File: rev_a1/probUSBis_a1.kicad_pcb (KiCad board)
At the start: 2 copper layers, 44.5 x 22.9 mm, 23 parts, among them CON1 USB-MINI-B, IC1 ATTINY85-P, P1 USB_A_MALE, P2 CONN_8, P3 CONN_4, U1 LM78L05ACZ

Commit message: moving usb around, fiddling with the pcb
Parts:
- JP1: moved to B.Cu
- moved P1 6.34 mm to (109.8, 100.5)
- moved CON1 4.06 mm to (109.2, 108.0)
- moved JP2 1.79 mm to (128.5, 93.0)
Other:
- board text added: "3.6V"
- board text added: "5V"
- board text added: "P1_LED"
- board text added: "VIN"
- board text added: "Voltage Select ->"
- board text added: "user LED jumper"
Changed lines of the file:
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@@
   (general
     (links 52)
-    (no_connects 52)
-    (area 93.996934 90.096623 152.40127 115.23345)
+    (no_connects 51)
+    (area 95.266934 89.249956 152.40127 115.26478)
     (thickness 1.6)
-    (drawings 12)
+    (drawings 22)
     (tracks 0)
     (zones 0)
@@
   )
   (module USB_MINI_B (layer F.Cu)
-    (at 110.49 104.14)
+    (at 109.22 108)
     (descr "USB Mini-B 5-pin SMD connector")
     (tags "USB, Mini-B, connector")
@@
   )
   (module PIN_ARRAY_3X1 (layer F.Cu)
-    (at 127 93.98)
+    (at 128.5 93)
     (descr "Connecteur 3 pins")
     (tags "CONN DEV")
@@
   )
   (module USB_A (layer F.Cu)
-    (at 111.2 106.68 180)
+    (at 109.8 100.5 180)
     (fp_text reference P1 (at 7.62 2.54 180) (layer F.SilkS)
       (effects (font (thickness 0.3048)))
@@
     )
   )
-  (module SM0603 (layer F.Cu)
+  (module SM0603 (layer B.Cu)
     (at 137.16 104.14 90)
     (attr smd)
-    (fp_text reference JP1 (at 0 0 90) (layer F.SilkS)
-      (effects (font (size 0.508 0.4572) (thickness 0.1143)))
-    )
-    (fp_text value JUMPER (at 0 0 90) (layer F.SilkS) hide
-      (effects (font (size 0.508 0.4572) (thickness 0.1143)))
-    )
-    (fp_line (start -1.143 -0.635) (end 1.143 -0.635) (layer F.SilkS) (width 0.127))
-    (fp_line (start 1.143 -0.635) (end 1.143 0.635) (layer F.SilkS) (width 0.127))
-    (fp_line (start 1.143 0.635) (end -1.143 0.635) (layer F.SilkS) (width 0.127))
-    (fp_line (start -1.143 0.635) (end -1.143 -0.635) (layer F.SilkS) (width 0.127))
+    (fp_text reference JP1 (at 0 0 90) (layer B.SilkS)
+      (effects (font (size 0.508 0.4572) (thickness 0.1143)) (justify mirror))
+    )
+    (fp_text value JUMPER (at 0 0 90) (layer B.SilkS) hide
+      (effects (font (size 0.508 0.4572) (thickness 0.1143)) (justify mirror))
+    )
+    (fp_line (start -1.143 0.635) (end 1.143 0.635) (layer B.SilkS) (width 0.127))
+    (fp_line (start 1.143 0.635) (end 1.143 -0.635) (layer B.SilkS) (width 0.127))
+    (fp_line (start 1.143 -0.635) (end -1.143 -0.635) (layer B.SilkS) (width 0.127))
+    (fp_line (start -1.143 -0.635) (end -1.143 0.635) (layer B.SilkS) (width 0.127))
     (pad 1 smd rect (at -0.762 0 90) (size 0.635 1.143)
-      (layers F.Cu F.Paste F.Mask)
+      (layers B.Cu B.Paste B.Mask)
       (net 16 N-000007)
     )
     (pad 2 smd rect (at 0.762 0 90) (size 0.635 1.143)
-      (layers F.Cu F.Paste F.Mask)
+      (layers B.Cu B.Paste B.Mask)
       (net 4 N-0000010)
     )
@@
     )
   )
+  (gr_text P1_LED (at 139.5 103) (layer F.SilkS)
+    (effects (font (size 1 1) (thickness 0.25)))
+  )
+  (gr_text "Voltage Select ->" (at 120 92.5) (layer F.SilkS)
+    (effects (font (size 0.6 0.6) (thickness 0.1)))
+  )
+  (gr_text 3.6V (at 131.4 95) (layer F.SilkS)
+    (effects (font (size 0.8 0.8) (thickness 0.1)))
+  )
+  (gr_text VCC (at 128.5 95) (layer F.SilkS)
+    (effects (font (size 0.8 0.8) (thickness 0.1)))
+  )
+  (gr_text 5V (at 126 95) (layer F.SilkS)
+    (effects (font (size 0.8 0.8) (thickness 0.1)))
+  )
+  (gr_text VIN (at 143.5 109.8) (layer F.SilkS)
+    (effects (font (size 0.8 0.8) (thickness 0.1)))
+  )
+  (gr_text GND (at 141 109.8) (layer F.SilkS)
+    (effects (font (size 0.8 0.8) (thickness 0.1)))
+  )
+  (gr_text "user LED \njumper" (at 139.7 104.14 270) (layer B.SilkS)
+    (effects (font (size 0.8 0.8) (thickness 0.1)) (justify mirror))
+  )
+  (gr_text 5V (at 138.5 109.9) (layer F.SilkS)
+    (effects (font (size 0.8 0.8) (thickness 0.1)))
+  )
+  (gr_text 3.6V (at 136 109.8) (layer F.SilkS)
+    (effects (font (size 0.8 0.8) (thickness 0.1)))
+  )
   (gr_text VCC (at 146 111.76 90) (layer F.SilkS)

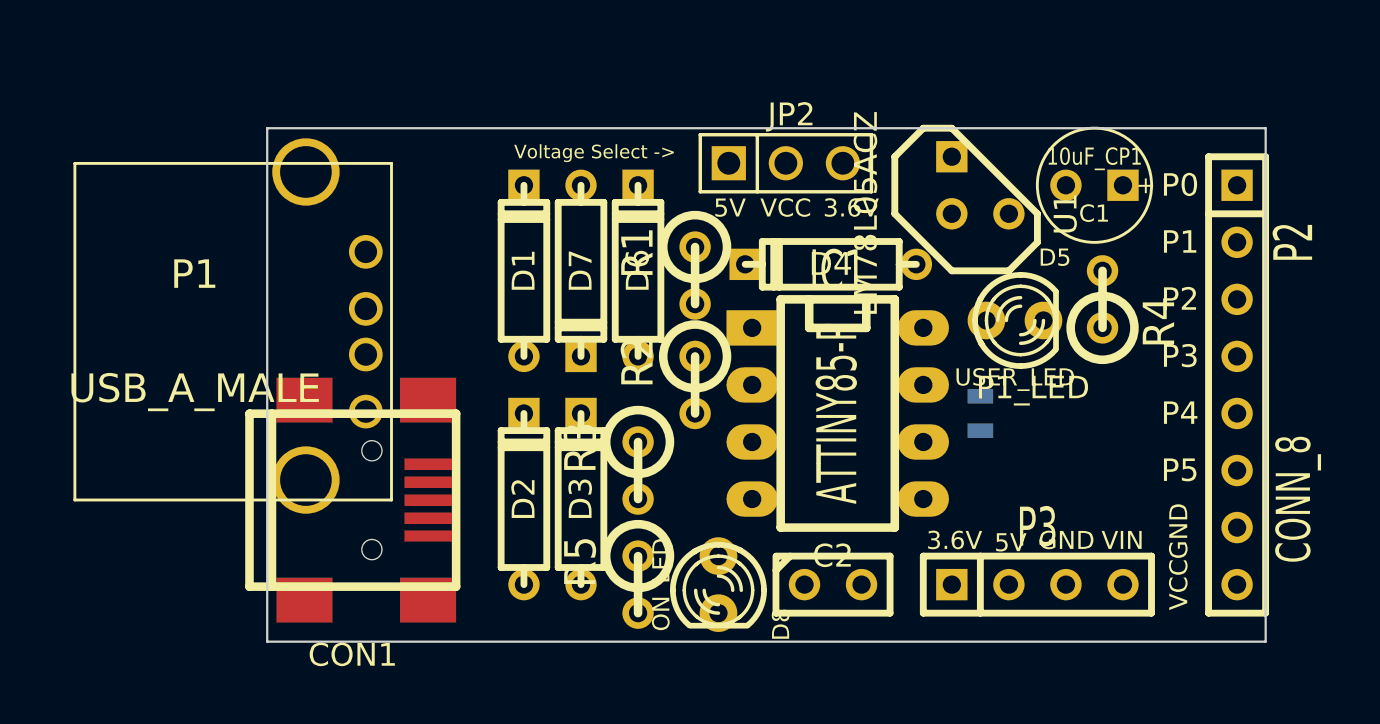
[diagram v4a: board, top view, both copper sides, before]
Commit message: moved stuff around, fixed 5v ref layout
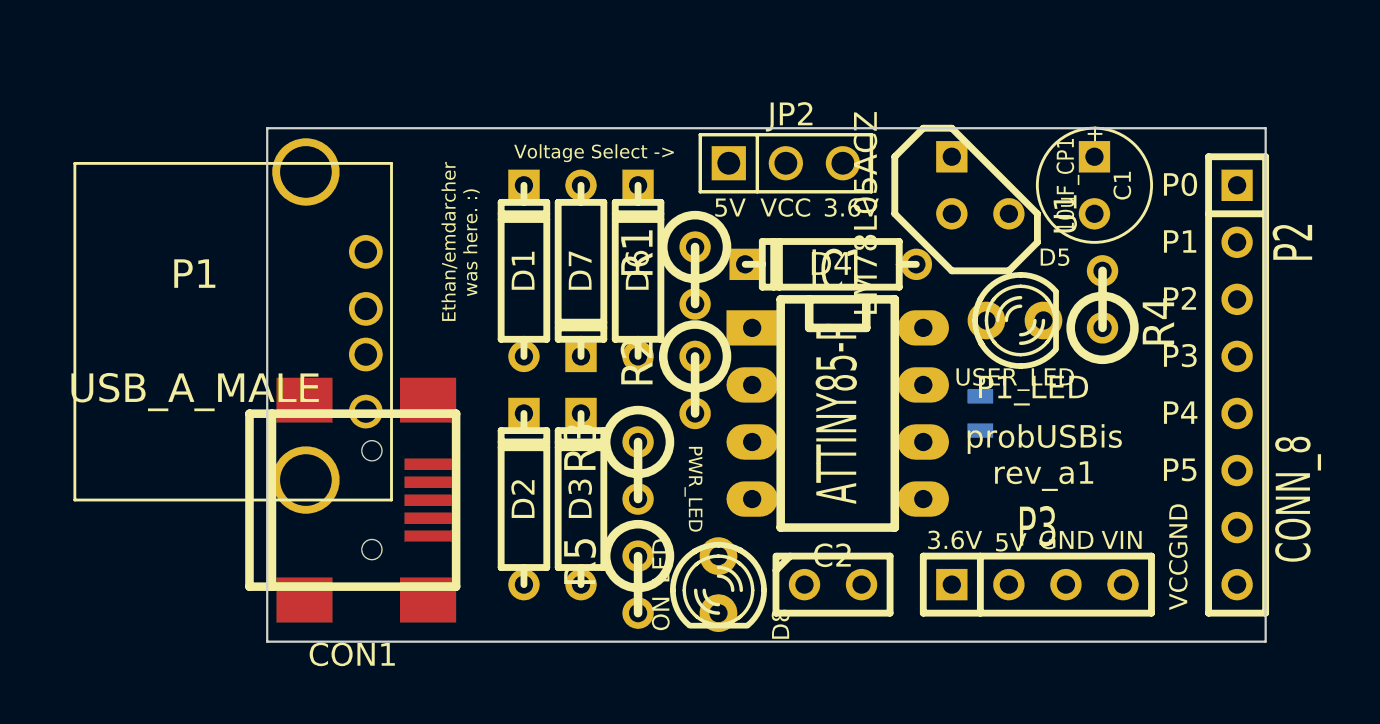
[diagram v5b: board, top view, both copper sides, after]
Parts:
- U1: footprint TO92-123 -> TO92
- turned C1 to 270 degrees
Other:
- board text added: "Ethan/emdarcher was here. :)"
- board text added: "P1_LED jumper"
- board text added: "PWR_LED"
- board text added: "probUSBis rev_a1"
- board text removed: "user LED jumper"
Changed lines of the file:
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@@
   (general
     (links 52)
-    (no_connects 51)
-    (area 95.266934 89.249956 152.40127 115.26478)
+    (no_connects 52)
+    (area 105.359999 91.389999 149.910001 114.350001)
     (thickness 1.6)
-    (drawings 22)
+    (drawings 25)
     (tracks 0)
     (zones 0)
@@
   )
   (module C1V5 (layer F.Cu)
-    (at 142.24 93.98 180)
+    (at 142.24 93.98 270)
     (descr "Condensateur e = 1 pas")
     (tags C)
-    (fp_text reference C1 (at 0 -1.26746 180) (layer F.SilkS)
+    (fp_text reference C1 (at 0 -1.26746 270) (layer F.SilkS)
       (effects (font (size 0.762 0.762) (thickness 0.127)))
     )
-    (fp_text value 10uF_CP1 (at 0 1.27 180) (layer F.SilkS)
+    (fp_text value 10uF_CP1 (at 0 1.27 270) (layer F.SilkS)
       (effects (font (size 0.762 0.635) (thickness 0.127)))
     )
-    (fp_text user + (at -2.286 0 180) (layer F.SilkS)
+    (fp_text user + (at -2.286 0 270) (layer F.SilkS)
       (effects (font (size 0.762 0.762) (thickness 0.2032)))
     )
     (fp_circle (center 0 0) (end 0.127 -2.54) (layer F.SilkS) (width 0.127))
-    (pad 1 thru_hole rect (at -1.27 0 180) (size 1.397 1.397) (drill 0.8128)
+    (pad 1 thru_hole rect (at -1.27 0 270) (size 1.397 1.397) (drill 0.8128)
       (layers *.Cu *.Mask F.SilkS)
       (net 20 VIN)
     )
-    (pad 2 thru_hole circle (at 1.27 0 180) (size 1.397 1.397) (drill 0.8128)
+    (pad 2 thru_hole circle (at 1.27 0 270) (size 1.397 1.397) (drill 0.8128)
       (layers *.Cu *.Mask F.SilkS)
       (net 3 GND)
@@
     )
   )
-  (module TO92-123 (layer F.Cu)
+  (module SM0603 (layer B.Cu)
+    (at 137.16 104.14 90)
+    (attr smd)
+    (fp_text reference JP1 (at 0 0 90) (layer B.SilkS)
+      (effects (font (size 0.508 0.4572) (thickness 0.1143)) (justify mirror))
+    )
+    (fp_text value JUMPER (at 0 0 90) (layer B.SilkS) hide
+      (effects (font (size 0.508 0.4572) (thickness 0.1143)) (justify mirror))
+    )
+    (fp_line (start -1.143 0.635) (end 1.143 0.635) (layer B.SilkS) (width 0.127))
+    (fp_line (start 1.143 0.635) (end 1.143 -0.635) (layer B.SilkS) (width 0.127))
+    (fp_line (start 1.143 -0.635) (end -1.143 -0.635) (layer B.SilkS) (width 0.127))
+    (fp_line (start -1.143 -0.635) (end -1.143 0.635) (layer B.SilkS) (width 0.127))
+    (pad 1 smd rect (at -0.762 0 90) (size 0.635 1.143)
+      (layers B.Cu B.Paste B.Mask)
+      (net 16 N-000007)
+    )
+    (pad 2 smd rect (at 0.762 0 90) (size 0.635 1.143)
+      (layers B.Cu B.Paste B.Mask)
+      (net 4 N-0000010)
+    )
+    (model smd\resistors\R0603.wrl
+      (at (xyz 0 0 0.001))
+      (scale (xyz 0.5 0.5 0.5))
+      (rotate (xyz 0 0 0))
+    )
+  )
+  (module TO92 (layer F.Cu)
     (at 137.16 93.98 90)
     (descr "Transistor TO92 brochage type BC237")
@@
     (fp_line (start -3.81 1.27) (end -2.54 2.54) (layer F.SilkS) (width 0.3048))
     (fp_line (start -2.54 2.54) (end -1.27 2.54) (layer F.SilkS) (width 0.3048))
-    (pad 3 thru_hole rect (at 1.27 -1.27 90) (size 1.397 1.397) (drill 0.8128)
+    (pad 1 thru_hole rect (at 1.27 -1.27 90) (size 1.397 1.397) (drill 0.8128)
+      (layers *.Cu *.Mask F.SilkS)
+      (net 20 VIN)
+    )
+    (pad 2 thru_hole circle (at -1.27 -1.27 90) (size 1.397 1.397) (drill 0.8128)
+      (layers *.Cu *.Mask F.SilkS)
+      (net 3 GND)
+    )
+    (pad 3 thru_hole circle (at -1.27 1.27 90) (size 1.397 1.397) (drill 0.8128)
       (layers *.Cu *.Mask F.SilkS)
       (net 8 N-0000016)
     )
-    (pad 2 thru_hole circle (at -1.27 -1.27 90) (size 1.397 1.397) (drill 0.8128)
-      (layers *.Cu *.Mask F.SilkS)
-      (net 3 GND)
-    )
-    (pad 1 thru_hole circle (at -1.27 1.27 90) (size 1.397 1.397) (drill 0.8128)
-      (layers *.Cu *.Mask F.SilkS)
-      (net 20 VIN)
-    )
     (model discret/to98.wrl
       (at (xyz 0 0 0))
@@
     )
   )
-  (module SM0603 (layer B.Cu)
-    (at 137.16 104.14 90)
-    (attr smd)
-    (fp_text reference JP1 (at 0 0 90) (layer B.SilkS)
-      (effects (font (size 0.508 0.4572) (thickness 0.1143)) (justify mirror))
-    )
-    (fp_text value JUMPER (at 0 0 90) (layer B.SilkS) hide
-      (effects (font (size 0.508 0.4572) (thickness 0.1143)) (justify mirror))
-    )
-    (fp_line (start -1.143 0.635) (end 1.143 0.635) (layer B.SilkS) (width 0.127))
-    (fp_line (start 1.143 0.635) (end 1.143 -0.635) (layer B.SilkS) (width 0.127))
-    (fp_line (start 1.143 -0.635) (end -1.143 -0.635) (layer B.SilkS) (width 0.127))
-    (fp_line (start -1.143 -0.635) (end -1.143 0.635) (layer B.SilkS) (width 0.127))
-    (pad 1 smd rect (at -0.762 0 90) (size 0.635 1.143)
-      (layers B.Cu B.Paste B.Mask)
-      (net 16 N-000007)
-    )
-    (pad 2 smd rect (at 0.762 0 90) (size 0.635 1.143)
-      (layers B.Cu B.Paste B.Mask)
-      (net 4 N-0000010)
-    )
-    (model smd\resistors\R0603.wrl
-      (at (xyz 0 0 0.001))
-      (scale (xyz 0.5 0.5 0.5))
-      (rotate (xyz 0 0 0))
-    )
+  (gr_text "Ethan/emdarcher \nwas here. :)" (at 114 96.52 90) (layer F.SilkS)
+    (effects (font (size 0.6 0.6) (thickness 0.15)))
+  )
+  (gr_text "probUSBis\nrev_a1" (at 140 106) (layer F.SilkS)
+    (effects (font (size 1 1) (thickness 0.25)))
+  )
+  (gr_text PWR_LED (at 124.46 107.5 270) (layer F.SilkS)
+    (effects (font (size 0.6 0.6) (thickness 0.15)))
   )
   (gr_text P1_LED (at 139.5 103) (layer F.SilkS)
@@
     (effects (font (size 0.8 0.8) (thickness 0.1)))
   )
-  (gr_text "user LED \njumper" (at 139.7 104.14 270) (layer B.SilkS)
+  (gr_text "P1_LED \njumper" (at 139.7 104.14 270) (layer B.SilkS)
     (effects (font (size 0.8 0.8) (thickness 0.1)) (justify mirror))
   )

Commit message: did some routing with freerouter
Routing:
- net GND: track 0.00 -> 90.3 mm
- net N-0000015: track 0.00 -> 56.4 mm
- net VCC: track 0.00 -> 54.6 mm
- net +5V: track 0.00 -> 39.6 mm, vias 0 -> 1
- net N-0000020: track 0.00 -> 39.5 mm
- net N-000006: track 0.00 -> 32.6 mm
- net +3.3V: track 0.00 -> 31.1 mm
- net VIN: track 0.00 -> 26.4 mm
- net N-0000019: track 0.00 -> 26.0 mm
- net N-000007: track 0.00 -> 25.0 mm
- net N-000002: track 0.00 -> 25.0 mm, vias 0 -> 1
- net N-0000017: track 0.00 -> 23.6 mm
- net N-000005: track 0.00 -> 16.4 mm
- net N-000008: track 0.00 -> 15.5 mm
- net N-0000016: track 0.00 -> 5.05 mm
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
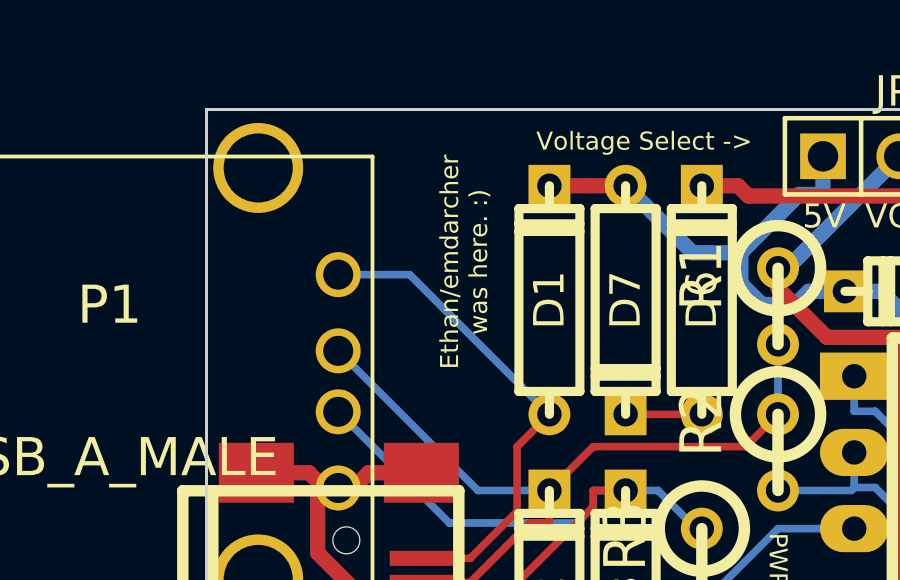
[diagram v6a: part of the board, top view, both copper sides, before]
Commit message: adding more info to back silkscreen
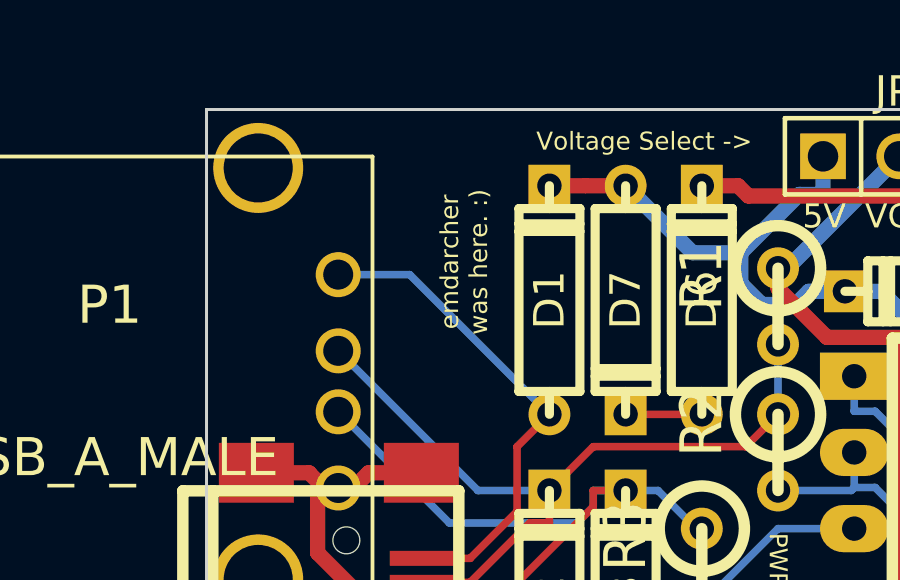
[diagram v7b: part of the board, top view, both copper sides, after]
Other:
- board text added: "CS,pin3"
- board text added: "DI SDA AREF,PWM"
- board text added: "MISO"
- board text added: "MOSI"
- board text added: "P1 D0 PWM"
- board text added: "P2 D/A SCL"
- board text added: "P3 D/A USB+"
- board text added: "P4 PWM D/A USB-"
- board text added: "P5 D/A RST"
- board text added: "SCK"
- board text added: "emdarcher was here. :)"
- board text added: "github.com/emdarcher/probUSBis_hardware"
- board text added: "pin4"
- board text removed: "Ethan/emdarcher was here. :)"
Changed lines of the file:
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@@
   (general
     (links 52)
-    (no_connects 52)
+    (no_connects 1)
     (area 93.306934 89.249956 152.40127 115.76478)
     (thickness 1.6)
-    (drawings 25)
+    (drawings 40)
     (tracks 183)
     (zones 0)
@@
     )
   )
-  (gr_text "Ethan/emdarcher \nwas here. :)" (at 114 96.52 90) (layer F.SilkS)
+  (gr_text SCK (at 143.51 99.06 270) (layer B.SilkS)
+    (effects (font (size 0.4 0.4) (thickness 0.1)) (justify mirror))
+  )
+  (gr_text pin4 (at 148.59 92 180) (layer B.SilkS)
+    (effects (font (size 0.4 0.4) (thickness 0.1)) (justify mirror))
+  )
+  (gr_text CS,pin3 (at 143.51 106.68 270) (layer B.SilkS)
+    (effects (font (size 0.4 0.4) (thickness 0.1)) (justify mirror))
+  )
+  (gr_text MISO (at 143.51 96.52 270) (layer B.SilkS)
+    (effects (font (size 0.4 0.4) (thickness 0.1)) (justify mirror))
+  )
+  (gr_text MOSI (at 143.51 93.98 270) (layer B.SilkS)
+    (effects (font (size 0.4 0.4) (thickness 0.1)) (justify mirror))
+  )
+  (gr_text VCC (at 146.05 111.76 270) (layer B.SilkS)
+    (effects (font (size 0.8 0.8) (thickness 0.16)) (justify mirror))
+  )
+  (gr_text GND (at 146.05 109.22 270) (layer B.SilkS)
+    (effects (font (size 0.8 0.8) (thickness 0.16)) (justify mirror))
+  )
+  (gr_text github.com/emdarcher/probUSBis_hardware (at 113.03 102.87 90) (layer B.SilkS)
+    (effects (font (size 0.6 0.6) (thickness 0.12)) (justify mirror))
+  )
+  (gr_text "DI\nSDA\n   AREF,PWM" (at 144.78 93.98 180) (layer B.SilkS)
+    (effects (font (size 0.6 0.6) (thickness 0.12)) (justify mirror))
+  )
+  (gr_text "P0\n\n\n" (at 146.05 93.98 270) (layer B.SilkS)
+    (effects (font (size 0.6 0.6) (thickness 0.12)) (justify mirror))
+  )
+  (gr_text "P1\nD0\nPWM" (at 146.05 96.52 270) (layer B.SilkS)
+    (effects (font (size 0.6 0.6) (thickness 0.12)) (justify mirror))
+  )
+  (gr_text "P2\nD/A\nSCL\n" (at 146.05 99.06 270) (layer B.SilkS)
+    (effects (font (size 0.6 0.6) (thickness 0.12)) (justify mirror))
+  )
+  (gr_text "P3\nD/A\nUSB+" (at 146.05 101.6 270) (layer B.SilkS)
+    (effects (font (size 0.6 0.6) (thickness 0.12)) (justify mirror))
+  )
+  (gr_text "P4 \nPWM\nD/A\nUSB-" (at 146.05 104.14 270) (layer B.SilkS)
+    (effects (font (size 0.6 0.6) (thickness 0.12)) (justify mirror))
+  )
+  (gr_text "P5 \nD/A\nRST" (at 146.05 106.68 270) (layer B.SilkS)
+    (effects (font (size 0.6 0.6) (thickness 0.12)) (justify mirror))
+  )
+  (gr_text "emdarcher \nwas here. :)" (at 114 96.52 90) (layer F.SilkS)
     (effects (font (size 0.6 0.6) (thickness 0.15)))
   )

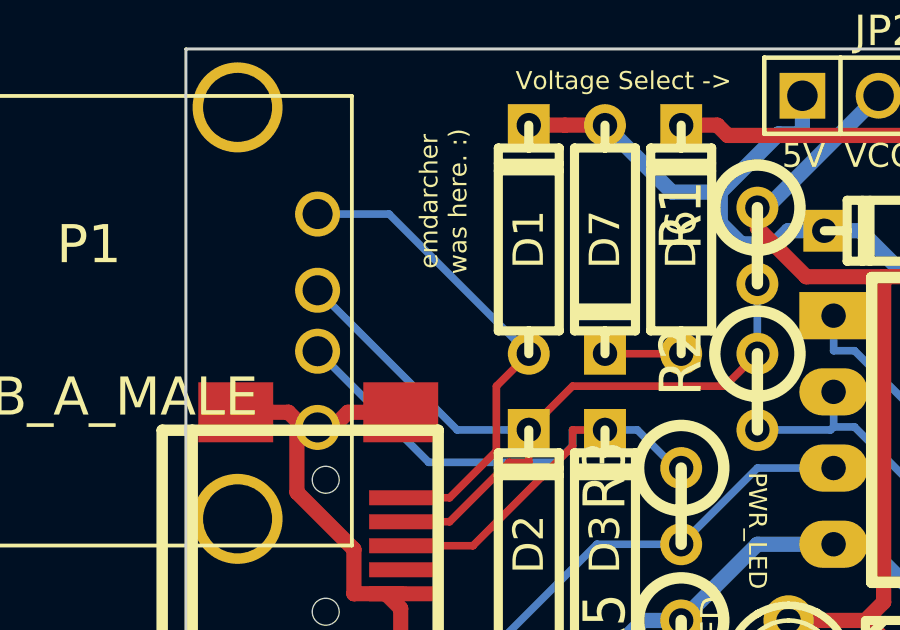
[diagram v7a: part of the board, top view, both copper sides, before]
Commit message: added logo on back of pcb, flipped
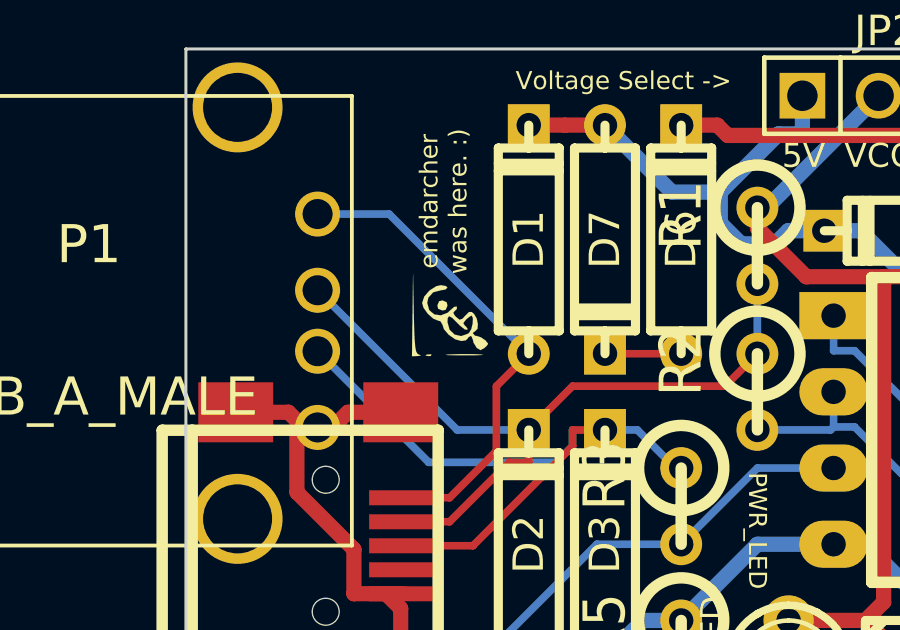
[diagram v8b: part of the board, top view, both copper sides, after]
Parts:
- added G***: LOGO, LOGO, F.Cu at (114.3, 100.3)
- added G***: LOGO, LOGO, B.Cu at (130.8, 101.6)
